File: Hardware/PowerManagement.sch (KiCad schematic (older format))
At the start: 11 parts, among them J7 10103594-0001LF, U10 Vreg

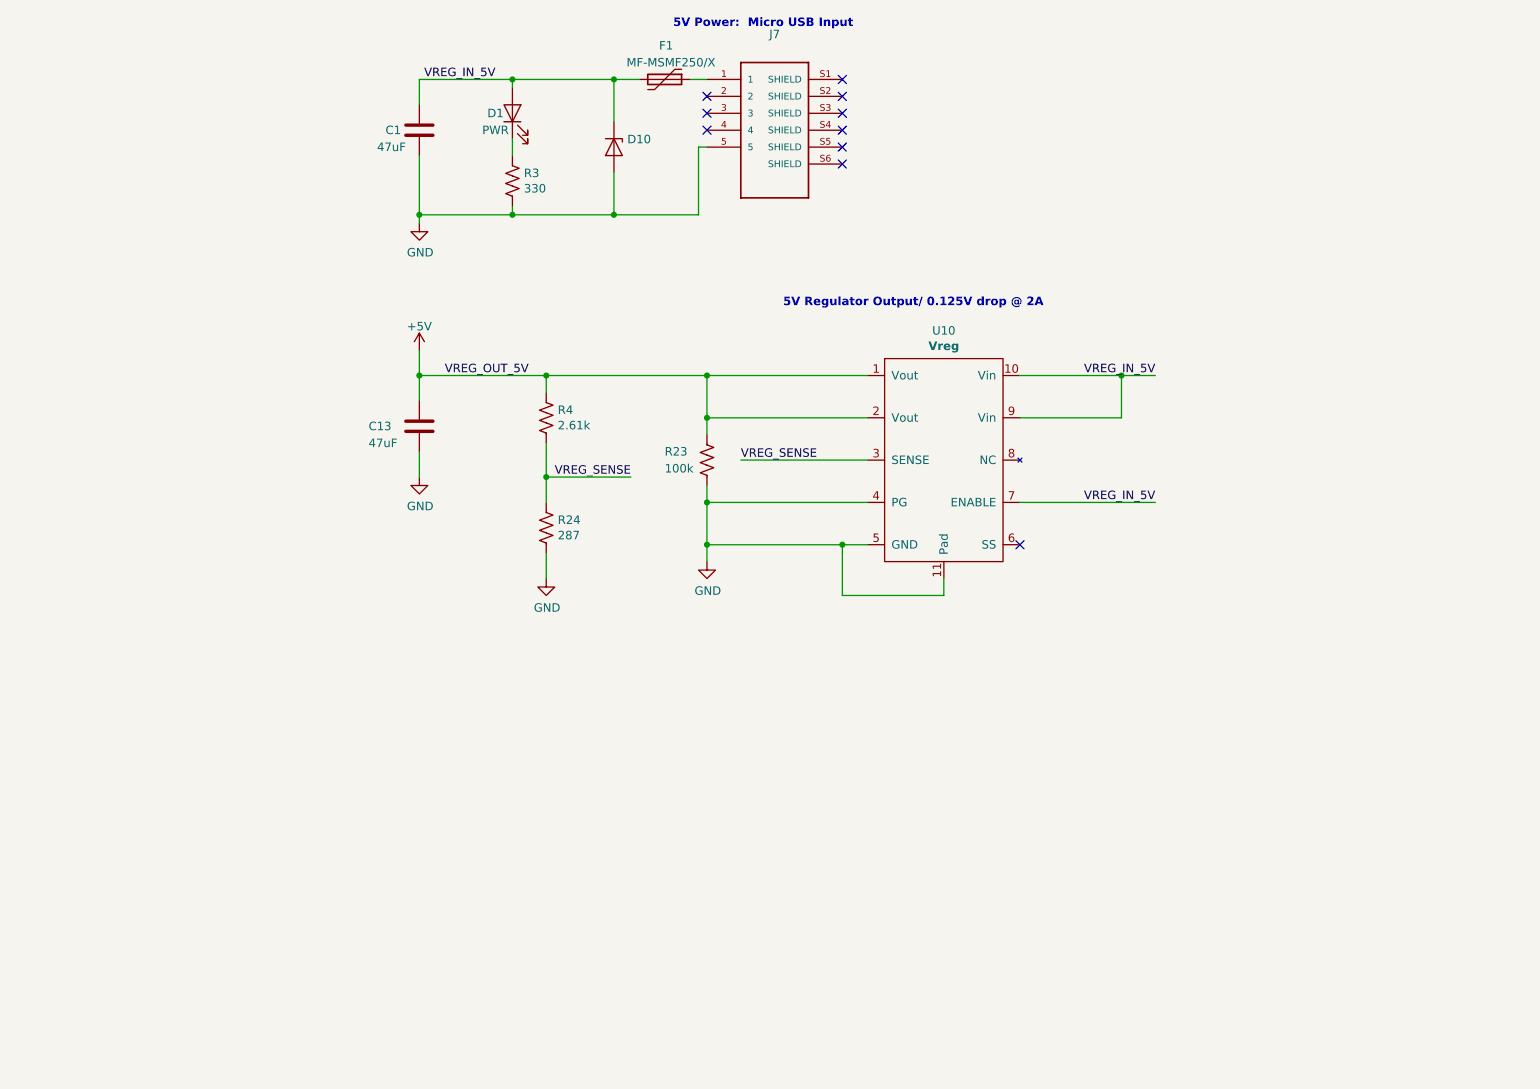
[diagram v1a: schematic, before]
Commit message: Up Changed I2C addres for DAC and ADC.  Added MOSFET to USART RX.
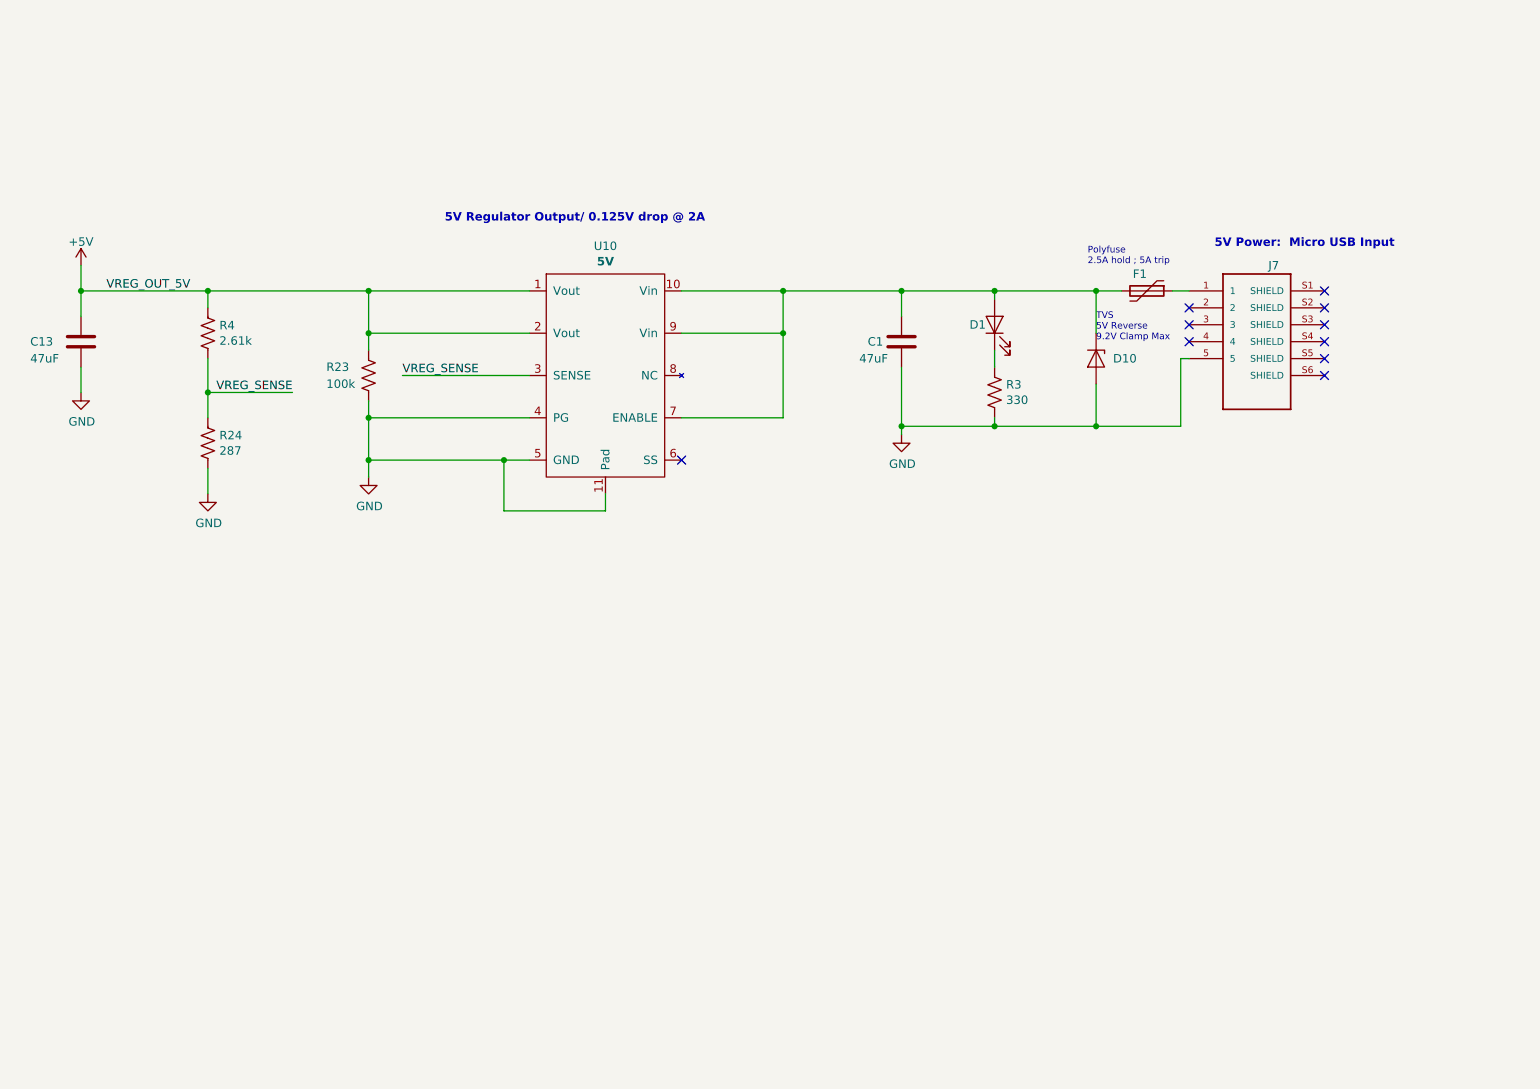
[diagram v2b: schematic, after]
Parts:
- U10: value Vreg -> 5V
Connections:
- net VREG_IN_5V: no longer names the net of C1.1, D1.2 (A), D10.1, F1.2, U10.10 (Vin), U10.7 (ENABLE), U10.9 (Vin)
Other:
- note added: "Polyfuse\n2.5A hold ; 5A trip"
- note added: "TVS\n5V Reverse\n9.2V Clamp Max"
- moved on the sheet: C1, C13, D1, D10, F1, J7, R23, R24, R3, R4, U10

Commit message: Updated Schematic Attribution and Documentation
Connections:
- net labels removed: VREG_OUT_5V
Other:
- note added: "5V Regulator (0.125V drop @ 2A)"
- note added: "The micro-USB power input was inspired by reading\nthe documents on the Raspberry Pi 3 B+ at the\nfollowing link (Upper Left Hand Corner of Schematic):\nhttps://www.raspberrypi.org/documentation/hardware/raspberrypi/schematics/rpi_SCH_3bplus_1p0_reduced.pdf\n\nLicense:\nhttps://www.raspberrypi.org/creative-commons/\n\nNo changes except for the voltage regulator \nthat the micro-USB input feeds in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"
- note removed: "5V Regulator Output/ 0.125V drop @ 2A"
- moved on the sheet: C1, C13, D1, D10, F1, J7, R23, R24, R3, R4, U10
